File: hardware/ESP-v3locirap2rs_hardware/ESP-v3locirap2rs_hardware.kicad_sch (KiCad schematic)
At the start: 1 part, among them U1 ESP32-WROOM-32

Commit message: directory changes
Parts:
- removed U1: ESP32-WROOM-32, RF_Module:ESP32-WROOM-32, symbol RF_Module:ESP32-WROOM-32
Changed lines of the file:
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@@
 	(generator_version "8.0")
 	(paper "A4")
-	(symbol
-		(lib_id "RF_Module:ESP32-WROOM-32")
-		(at 111.76 85.09 0)
-		(unit 1)
-		(exclude_from_sim no)
-		(in_bom yes)
-		(on_board yes)
-		(dnp no)
-		(fields_autoplaced yes)
-		(property "Reference" "U1"
-			(at 113.9541 46.99 0)
-			(effects
-				(font
-					(size 1.27 1.27)
-				)
-				(justify left)
-			)
-		)
-		(property "Value" "ESP32-WROOM-32"
-			(at 113.9541 49.53 0)
-			(effects
-				(font
-					(size 1.27 1.27)
-				)
-				(justify left)
-			)
-		)
-		(property "Footprint" "RF_Module:ESP32-WROOM-32"
-			(at 111.76 123.19 0)
-			(effects
-				(font
-					(size 1.27 1.27)
-				)
-				(hide yes)
-			)
-		)
-		(property "Datasheet" "https://www.espressif.com/sites/default/files/documentation/esp32-wroom-32_datasheet_en.pdf"
-			(at 104.14 83.82 0)
-			(effects
-				(font
-					(size 1.27 1.27)
-				)
-				(hide yes)
-			)
-		)
-		(property "Description" "RF Module, ESP32-D0WDQ6 SoC, Wi-Fi 802.11b/g/n, Bluetooth, BLE, 32-bit, 2.7-3.6V, onboard antenna, SMD"
-			(at 111.76 85.09 0)
-			(effects
-				(font
-					(size 1.27 1.27)
-				)
-				(hide yes)
-			)
-		)
-		(pin "17"
-		)
-		(pin "37"
-		)
-		(pin "30"
-		)
-		(pin "23"
-		)
-		(pin "33"
-		)
-		(pin "26"
-		)
-		(pin "22"
-		)
-		(pin "38"
-		)
-		(pin "1"
-		)
-		(pin "16"
-		)
-		(pin "11"
-		)
-		(pin "24"
-		)
-		(pin "25"
-		)
-		(pin "5"
-		)
-		(pin "9"
-		)
-		(pin "35"
-		)
-		(pin "27"
-		)
-		(pin "20"
-		)
-		(pin "3"
-		)
-		(pin "12"
-		)
-		(pin "29"
-		)
-		(pin "8"
-		)
-		(pin "4"
-		)
-		(pin "2"
-		)
-		(pin "32"
-		)
-		(pin "6"
-		)
-		(pin "14"
-		)
-		(pin "39"
-		)
-		(pin "36"
-		)
-		(pin "21"
-		)
-		(pin "7"
-		)
-		(pin "19"
-		)
-		(pin "28"
-		)
-		(pin "15"
-		)
-		(pin "10"
-		)
-		(pin "13"
-		)
-		(pin "18"
-		)
-		(pin "34"
-		)
-		(pin "31"
-		)
-		(instances
-			(project ""
-				(path "/1e8ac7e4-9b26-4abc-8f5a-d72e2e725c2d"
-					(reference "U1")
-					(unit 1)
-				)
-			)
-		)
-	)
 	(sheet_instances
 		(path "/"

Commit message: gyroscope updates
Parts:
- added U1: ESP32-DEVKITC-32D, digikey-footprints:MODULE_ESP32-DEVKITC-32D, symbol ESP32-DEVKITC-32D:ESP32-DEVKITC-32D

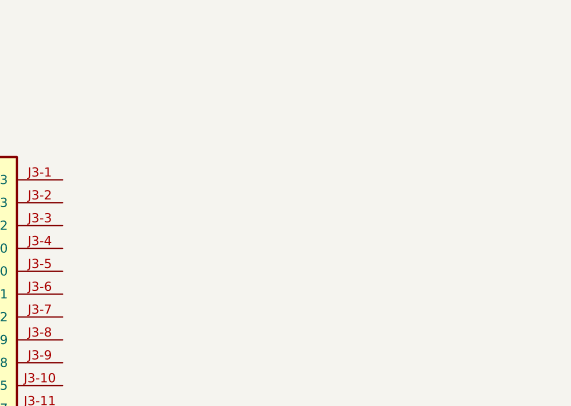
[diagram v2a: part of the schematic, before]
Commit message: changed keycad path?
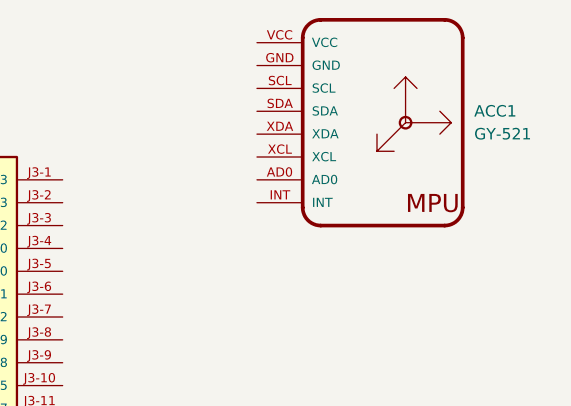
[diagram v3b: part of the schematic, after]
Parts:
- added ACC1: GY-521, ESP-v3locirap2rs_footprints:GY-521, symbol GY-521:GY-521
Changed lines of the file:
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@@
 	(paper "A4")
+	(symbol
+		(lib_id "GY-521:GY-521")
+		(at 199.39 74.93 0)
+		(unit 1)
+		(exclude_from_sim no)
+		(in_bom yes)
+		(on_board yes)
+		(dnp no)
+		(fields_autoplaced yes)
+		(property "Reference" "ACC1"
+			(at 207.01 73.6599 0)
+			(effects
+				(font
+					(size 1.27 1.27)
+				)
+				(justify left)
+			)
+		)
+		(property "Value" "GY-521"
+			(at 207.01 76.1999 0)
+			(effects
+				(font
+					(size 1.27 1.27)
+				)
+				(justify left)
+			)
+		)
+		(property "Footprint" "ESP-v3locirap2rs_footprints:GY-521"
+			(at 199.39 74.93 0)
+			(effects
+				(font
+					(size 1.27 1.27)
+				)
+				(hide yes)
+			)
+		)
+		(property "Datasheet" ""
+			(at 199.39 74.93 0)
+			(effects
+				(font
+					(size 1.27 1.27)
+				)
+				(hide yes)
+			)
+		)
+		(property "Description" ""
+			(at 199.39 74.93 0)
+			(effects
+				(font
+					(size 1.27 1.27)
+				)
+				(hide yes)
+			)
+		)
+		(property "MF" "GODREAM FORDREAM CO., LIMITED"
+			(at 199.39 74.93 0)
+			(effects
+				(font
+					(size 1.27 1.27)
+				)
+				(justify bottom)
+				(hide yes)
+			)
+		)
+		(property "Description_1" "\n                        \n                            Triple Axis Accelerometer Gyro Breakout\n                        \n"
+			(at 199.39 74.93 0)
+			(effects
+				(font
+					(size 1.27 1.27)
+				)
+				(justify bottom)
+				(hide yes)
+			)
+		)
+		(property "Package" "Package"
+			(at 199.39 74.93 0)
+			(effects
+				(font
+					(size 1.27 1.27)
+				)
+				(justify bottom)
+				(hide yes)
+			)
+		)
+		(property "Price" "None"
+			(at 199.39 74.93 0)
+			(effects
+				(font
+					(size 1.27 1.27)
+				)
+				(justify bottom)
+				(hide yes)
+			)
+		)
+		(property "SnapEDA_Link" "https://www.snapeda.com/parts/GY-521/GODREAM+FORDREAM+CO.%252C+LIMITED/view-part/?ref=snap"
+			(at 199.39 74.93 0)
+			(effects
+				(font
+					(size 1.27 1.27)
+				)
+				(justify bottom)
+				(hide yes)
+			)
+		)
+		(property "MP" "GY-521"
+			(at 199.39 74.93 0)
+			(effects
+				(font
+					(size 1.27 1.27)
+				)
+				(justify bottom)
+				(hide yes)
+			)
+		)
+		(property "Availability" "Not in stock"
+			(at 199.39 74.93 0)
+			(effects
+				(font
+					(size 1.27 1.27)
+				)
+				(justify bottom)
+				(hide yes)
+			)
+		)
+		(property "Check_prices" "https://www.snapeda.com/parts/GY-521/GODREAM+FORDREAM+CO.%252C+LIMITED/view-part/?ref=eda"
+			(at 199.39 74.93 0)
+			(effects
+				(font
+					(size 1.27 1.27)
+				)
+				(justify bottom)
+				(hide yes)
+			)
+		)
+		(pin "VCC"
+		)
+		(pin "SCL"
+		)
+		(pin "XCL"
+		)
+		(pin "AD0"
+		)
+		(pin "SDA"
+		)
+		(pin "XDA"
+		)
+		(pin "GND"
+		)
+		(pin "INT"
+		)
+		(instances
+			(project ""
+				(path "/1e8ac7e4-9b26-4abc-8f5a-d72e2e725c2d"
+					(reference "ACC1")
+					(unit 1)
+				)
+			)
+		)
+	)
 	(symbol
 		(lib_id "ESP32-DEVKITC-32D:ESP32-DEVKITC-32D")

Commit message: updates
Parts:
- removed ACC1: GY-521, ESP-v3locirap2rs_footprints:GY-521, symbol GY-521:GY-521
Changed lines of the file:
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@@
 	(paper "A4")
-	(symbol
-		(lib_id "GY-521:GY-521")
-		(at 199.39 74.93 0)
-		(unit 1)
-		(exclude_from_sim no)
-		(in_bom yes)
-		(on_board yes)
-		(dnp no)
-		(fields_autoplaced yes)
-		(property "Reference" "ACC1"
-			(at 207.01 73.6599 0)
-			(effects
-				(font
-					(size 1.27 1.27)
-				)
-				(justify left)
-			)
-		)
-		(property "Value" "GY-521"
-			(at 207.01 76.1999 0)
-			(effects
-				(font
-					(size 1.27 1.27)
-				)
-				(justify left)
-			)
-		)
-		(property "Footprint" "ESP-v3locirap2rs_footprints:GY-521"
-			(at 199.39 74.93 0)
-			(effects
-				(font
-					(size 1.27 1.27)
-				)
-				(hide yes)
-			)
-		)
-		(property "Datasheet" ""
-			(at 199.39 74.93 0)
-			(effects
-				(font
-					(size 1.27 1.27)
-				)
-				(hide yes)
-			)
-		)
-		(property "Description" ""
-			(at 199.39 74.93 0)
-			(effects
-				(font
-					(size 1.27 1.27)
-				)
-				(hide yes)
-			)
-		)
-		(property "MF" "GODREAM FORDREAM CO., LIMITED"
-			(at 199.39 74.93 0)
-			(effects
-				(font
-					(size 1.27 1.27)
-				)
-				(justify bottom)
-				(hide yes)
-			)
-		)
-		(property "Description_1" "\n                        \n                            Triple Axis Accelerometer Gyro Breakout\n                        \n"
-			(at 199.39 74.93 0)
-			(effects
-				(font
-					(size 1.27 1.27)
-				)
-				(justify bottom)
-				(hide yes)
-			)
-		)
-		(property "Package" "Package"
-			(at 199.39 74.93 0)
-			(effects
-				(font
-					(size 1.27 1.27)
-				)
-				(justify bottom)
-				(hide yes)
-			)
-		)
-		(property "Price" "None"
-			(at 199.39 74.93 0)
-			(effects
-				(font
-					(size 1.27 1.27)
-				)
-				(justify bottom)
-				(hide yes)
-			)
-		)
-		(property "SnapEDA_Link" "https://www.snapeda.com/parts/GY-521/GODREAM+FORDREAM+CO.%252C+LIMITED/view-part/?ref=snap"
-			(at 199.39 74.93 0)
-			(effects
-				(font
-					(size 1.27 1.27)
-				)
-				(justify bottom)
-				(hide yes)
-			)
-		)
-		(property "MP" "GY-521"
-			(at 199.39 74.93 0)
-			(effects
-				(font
-					(size 1.27 1.27)
-				)
-				(justify bottom)
-				(hide yes)
-			)
-		)
-		(property "Availability" "Not in stock"
-			(at 199.39 74.93 0)
-			(effects
-				(font
-					(size 1.27 1.27)
-				)
-				(justify bottom)
-				(hide yes)
-			)
-		)
-		(property "Check_prices" "https://www.snapeda.com/parts/GY-521/GODREAM+FORDREAM+CO.%252C+LIMITED/view-part/?ref=eda"
-			(at 199.39 74.93 0)
-			(effects
-				(font
-					(size 1.27 1.27)
-				)
-				(justify bottom)
-				(hide yes)
-			)
-		)
-		(pin "VCC"
-		)
-		(pin "SCL"
-		)
-		(pin "XCL"
-		)
-		(pin "AD0"
-		)
-		(pin "SDA"
-		)
-		(pin "XDA"
-		)
-		(pin "GND"
-		)
-		(pin "INT"
-		)
-		(instances
-			(project ""
-				(path "/1e8ac7e4-9b26-4abc-8f5a-d72e2e725c2d"
-					(reference "ACC1")
-					(unit 1)
-				)
-			)
-		)
-	)
 	(symbol
 		(lib_id "ESP32-DEVKITC-32D:ESP32-DEVKITC-32D")

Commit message: circuit diagrams
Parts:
- removed U1: ESP32-DEVKITC-32D, digikey-footprints:MODULE_ESP32-DEVKITC-32D, symbol ESP32-DEVKITC-32D:ESP32-DEVKITC-32D
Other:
- added sheet ESP32 (ESP32.kicad_sch)
- added sheet GY521 (GY521.kicad_sch)

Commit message: schematic finalization
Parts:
- added BAT1: BC9VPC, digikey-footprints:Battery_Holder_9V_BC9VPC-ND, symbol dk_Battery-Holders-Clips-Contacts:BC9VPC
- added U2: L7805CV, digikey-footprints:TO-220-3, symbol dk_PMIC-Voltage-Regulators-Linear:L7805CV
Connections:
- net GND: now also BAT1.POS, U2.2 (GND)
- new net: BAT1.NEG, U2.1 (IN)
- new net ESP32/5V: U2.3 (OUT)
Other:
- added sheet LCD-Screen (LCD-Screen.kicad_sch)
- sheet ESP32 ports: added 5V, Pin 15, Pin 16, Pin 17, Pin 18, Pin 19, Pin 23; removed none

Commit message: PCB completed
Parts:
- BAT1: footprint digikey-footprints:Battery_Holder_9V_BC9VPC-ND -> Battery:BatteryHolder_Eagle_12BH611-GR
- U2: footprint digikey-footprints:TO-220-3 -> Package_TO_SOT_THT:TO-220-3_Vertical
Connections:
- net GND: now also BAT1.NEG; no longer BAT1.POS
- net at U2.1 (IN): now also BAT1.POS; no longer BAT1.NEG
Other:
- moved on the sheet: BAT1
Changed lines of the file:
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@@
 			)
 		)
-		(property "Footprint" "digikey-footprints:TO-220-3"
+		(property "Footprint" "Package_TO_SOT_THT:TO-220-3_Vertical"
 			(at 137.16 132.08 0)
 			(effects
@@
 	(symbol
 		(lib_id "dk_Battery-Holders-Clips-Contacts:BC9VPC")
-		(at 116.84 137.16 0)
+		(at 116.84 137.16 180)
 		(unit 1)
 		(exclude_from_sim no)
@@
 		(fields_autoplaced yes)
 		(property "Reference" "BAT1"
-			(at 116.459 129.54 0)
+			(at 117.221 129.54 0)
 			(effects
 				(font
@@
 		)
 		(property "Value" "BC9VPC"
-			(at 116.459 132.08 0)
-			(effects
-				(font
-					(size 1.524 1.524)
-				)
-			)
-		)
-		(property "Footprint" "digikey-footprints:Battery_Holder_9V_BC9VPC-ND"
-			(at 121.92 132.08 0)
+			(at 117.221 132.08 0)
+			(effects
+				(font
+					(size 1.524 1.524)
+				)
+			)
+		)
+		(property "Footprint" "Battery:BatteryHolder_Eagle_12BH611-GR"
+			(at 111.76 142.24 0)
 			(effects
 				(font
@@
 		)
 		(property "Datasheet" "http://www.memoryprotectiondevices.com/datasheets/BC9VPC-datasheet.pdf"
-			(at 121.92 129.54 0)
+			(at 111.76 144.78 0)
 			(effects
 				(font
@@
 		)
 		(property "Digi-Key_PN" "BC9VPC-ND"
-			(at 121.92 127 0)
+			(at 111.76 147.32 0)
 			(effects
 				(font
@@
 		)
 		(property "MPN" "BC9VPC"
-			(at 121.92 124.46 0)
+			(at 111.76 149.86 0)
 			(effects
 				(font
@@
 		)
 		(property "Category" "Battery Products"
-			(at 121.92 121.92 0)
+			(at 111.76 152.4 0)
 			(effects
 				(font
@@
 		)
 		(property "Family" "Battery Holders, Clips, Contacts"
-			(at 121.92 119.38 0)
+			(at 111.76 154.94 0)
 			(effects
 				(font
@@
 		)
 		(property "DK_Datasheet_Link" "http://www.memoryprotectiondevices.com/datasheets/BC9VPC-datasheet.pdf"
-			(at 121.92 116.84 0)
+			(at 111.76 157.48 0)
 			(effects
 				(font
@@
 		)
 		(property "DK_Detail_Page" "/product-detail/en/mpd-memory-protection-devices/BC9VPC/BC9VPC-ND/257747"
-			(at 121.92 114.3 0)
+			(at 111.76 160.02 0)
 			(effects
 				(font
@@
 		)
 		(property "Description_1" "BATTERY HOLDER 9V PC PIN"
-			(at 121.92 111.76 0)
+			(at 111.76 162.56 0)
 			(effects
 				(font
@@
 		)
 		(property "Manufacturer" "MPD (Memory Protection Devices)"
-			(at 121.92 109.22 0)
+			(at 111.76 165.1 0)
 			(effects
 				(font
@@
 		)
 		(property "Status" "Active"
-			(at 121.92 106.68 0)
-			(effects
-				(font
+			(at 111.76 167.64 0)
+			(effects
+				(font

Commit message: pcb & schematic updates
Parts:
- removed BAT1: BC9VPC, Battery:BatteryHolder_Eagle_12BH611-GR, symbol dk_Battery-Holders-Clips-Contacts:BC9VPC
- removed U2: L7805CV, Package_TO_SOT_THT:TO-220-3_Vertical, symbol dk_PMIC-Voltage-Regulators-Linear:L7805CV
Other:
- added sheet Power-Supply (Power-Supply.kicad_sch)
